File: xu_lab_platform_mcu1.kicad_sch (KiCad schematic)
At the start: 22 parts, among them J1 SWD Connector, SW1 SW_Push, SW2 SW_SPDT, SW3 SW_SPDT, U1 STM32F446RCTx, Y1 25 MHz

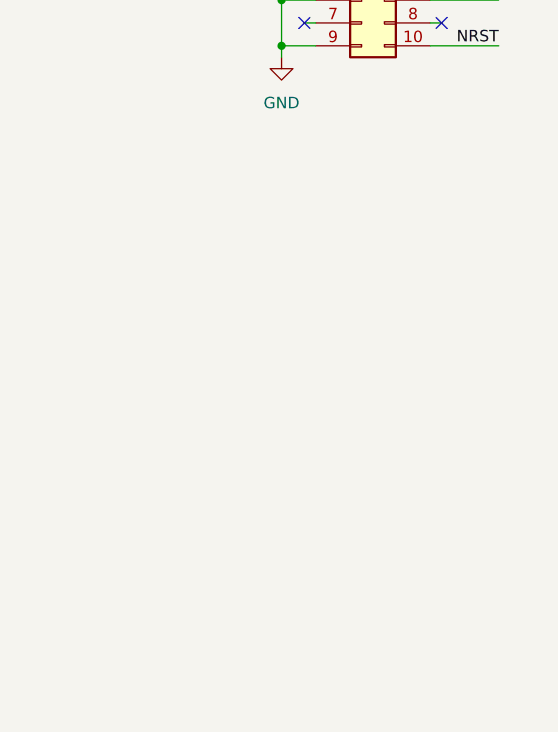
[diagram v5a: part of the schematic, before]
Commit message: Add pull up resistors for I2C pins
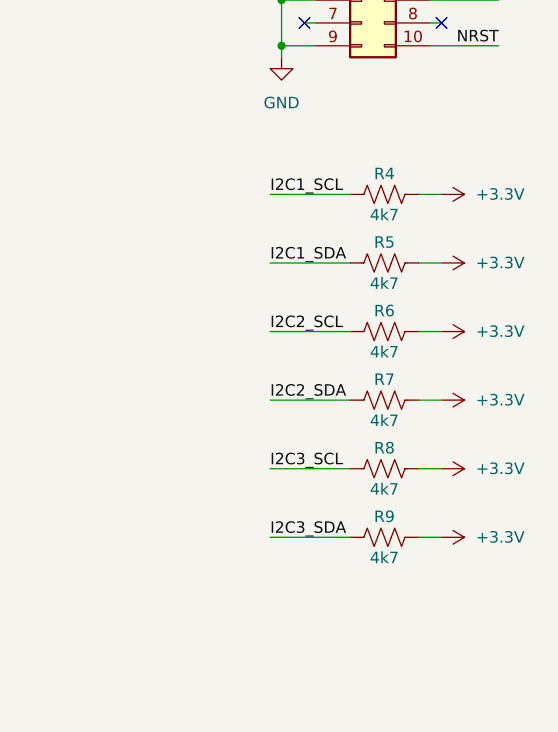
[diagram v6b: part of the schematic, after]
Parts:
- added R4, R5, R6, R7, R8, R9: 4k7, symbol Device:R_US
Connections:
- net +3.3V: now also R4.1, R5.1, R6.1, R7.1, R8.1, R9.1
- net I2C1_SCL: now also R4.2
- net I2C1_SDA: now also R5.2
- net I2C2_SCL: now also R6.2
- net I2C2_SDA: now also R7.2
- net I2C3_SCL: now also R8.2
- net I2C3_SDA: now also R9.2

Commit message: Update MCU A pin configuration with SPI CS and an LED output
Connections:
- net LED_OUT: now reaches U1.33 (PB12)
- net SPI1_CS1: now reaches U1.37 (PC6)
- no-connect marks 24 -> 22
